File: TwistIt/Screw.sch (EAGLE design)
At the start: 6 parts

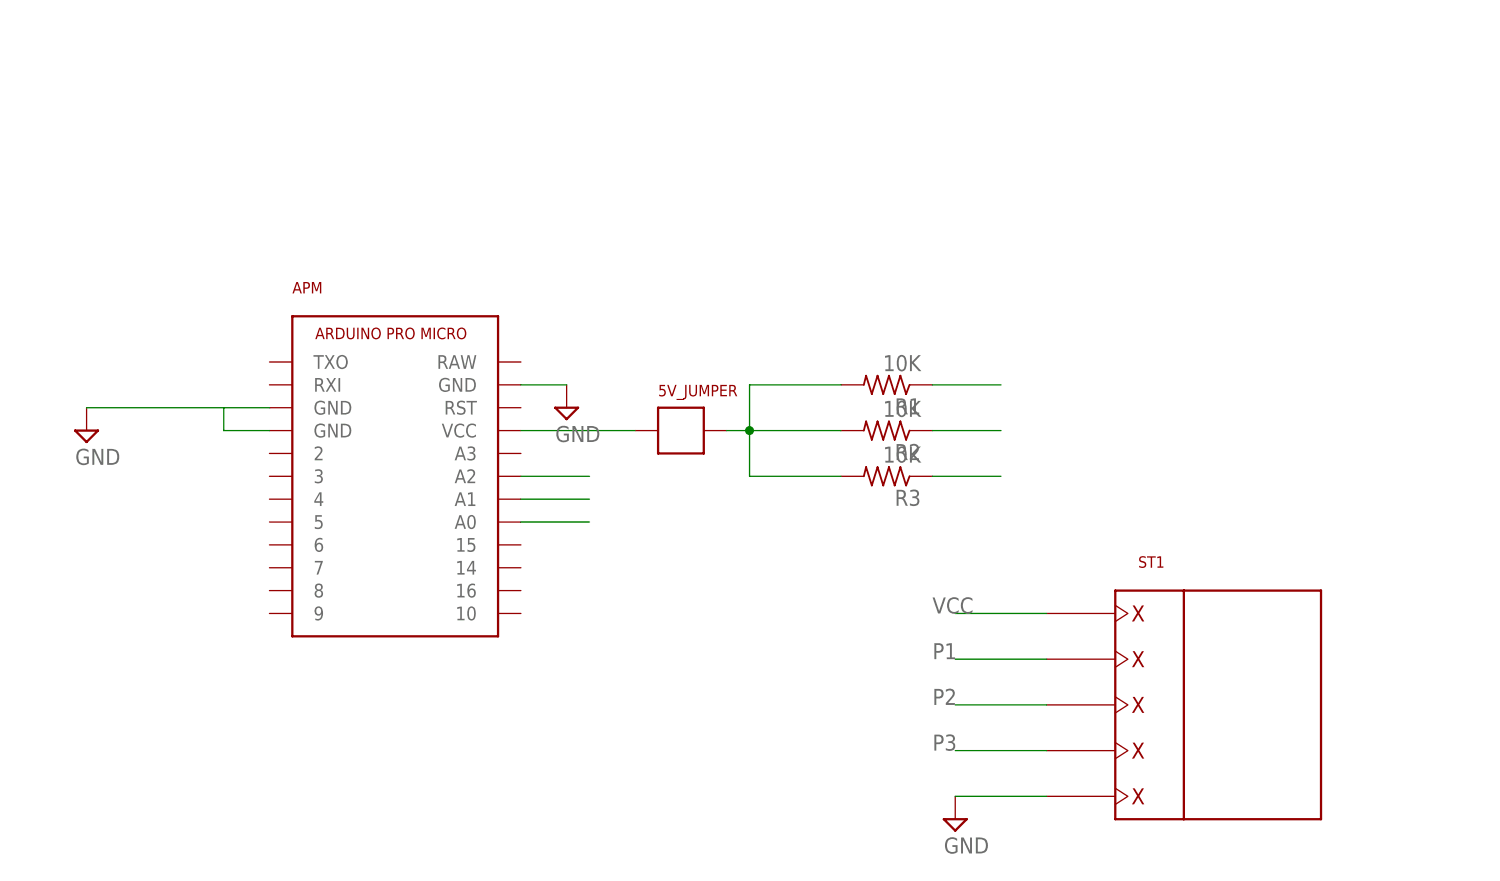
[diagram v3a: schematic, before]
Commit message: Add the yogi bear breakout board
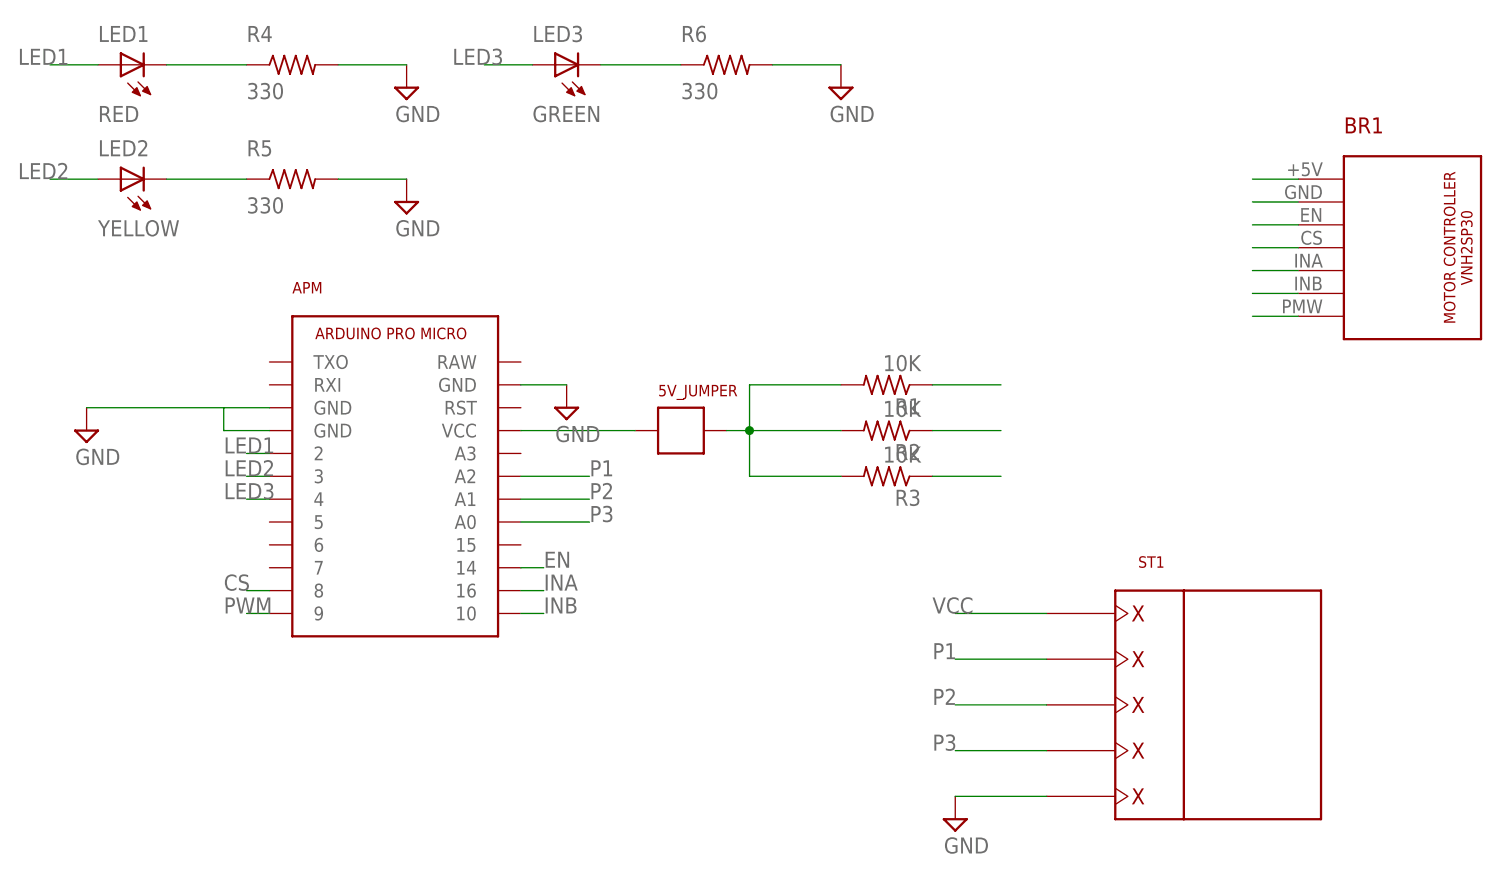
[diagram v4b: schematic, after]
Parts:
- added BR1: VNH2SP30_MOTOR_CONTROLLER, pie:VNH2SP30_MOTOR_CONTROLLER
- added LED1: RED, pie:LED-FKIT-1206
- added LED2: YELLOW, pie:LED-FKIT-1206
- added LED3: GREEN, pie:LED-FKIT-1206
- added R4, R5, R6: 330, pie:R-US_R0603
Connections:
- new net CS: APM.8, BR1.CS
- new net EN: APM.14, BR1.EN
- new net INA: APM.16, BR1.INA
- new net INB: APM.10, BR1.INB
- new net LED1: APM.2, LED1.A
- new net LED2: APM.3, LED2.A
- new net LED3: APM.4, LED3.A
- new net N$2: LED1.C, R4.1
- new net N$4: LED2.C, R5.1
- new net N$6: LED3.C, R6.1
- new net PWM: APM.9, BR1.PMW
- net GND: now also BR1.GND, R4.2, R5.2, R6.2
- net VCC: now also BR1.+5V
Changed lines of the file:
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@@
 <?xml version="1.0" encoding="utf-8"?>
 <!DOCTYPE eagle SYSTEM "eagle.dtd">
-<eagle version="7.6.0">
+<eagle version="7.7.0">
 <drawing>
 <settings>
@@
 <part name="SUPPLY3" library="pie" deviceset="GND" device=""/>
 <part name="5V_JUMPER" library="pie" deviceset="JUMPER" device=""/>
+<part name="BR1" library="pie" deviceset="VNH2SP30_MOTOR_CONTROLLER" device=""/>
+<part name="LED1" library="pie" deviceset="LED" device="-FKIT-1206" value="RED"/>
+<part name="R4" library="pie" deviceset="R-US_" device="R0603" value="330"/>
+<part name="SUPPLY4" library="pie" deviceset="GND" device=""/>
+<part name="LED2" library="pie" deviceset="LED" device="-FKIT-1206" value="YELLOW"/>
+<part name="R5" library="pie" deviceset="R-US_" device="R0603" value="330"/>
+<part name="SUPPLY5" library="pie" deviceset="GND" device=""/>
+<part name="LED3" library="pie" deviceset="LED" device="-FKIT-1206" value="GREEN"/>
+<part name="R6" library="pie" deviceset="R-US_" device="R0603" value="330"/>
+<part name="SUPPLY6" library="pie" deviceset="GND" device=""/>
 </parts>
 <sheets>
@@
 <instance part="SUPPLY3" gate="GND" x="81.28" y="101.6"/>
 <instance part="5V_JUMPER" gate="G$1" x="93.98" y="99.06"/>
+<instance part="BR1" gate="G$1" x="175.26" y="119.38"/>
+<instance part="LED1" gate="G$1" x="33.02" y="139.7"/>
+<instance part="R4" gate="G$1" x="50.8" y="139.7"/>
+<instance part="SUPPLY4" gate="GND" x="63.5" y="137.16"/>
+<instance part="LED2" gate="G$1" x="33.02" y="127"/>
+<instance part="R5" gate="G$1" x="50.8" y="127"/>
+<instance part="SUPPLY5" gate="GND" x="63.5" y="124.46"/>
+<instance part="LED3" gate="G$1" x="81.28" y="139.7"/>
+<instance part="R6" gate="G$1" x="99.06" y="139.7"/>
+<instance part="SUPPLY6" gate="GND" x="111.76" y="137.16"/>
 </instances>
 <busses>
@@
 <wire x1="81.28" y1="104.14" x2="76.2" y2="104.14" width="0.1524" layer="91"/>
 </segment>
+<segment>
+<pinref part="BR1" gate="G$1" pin="GND"/>
+<wire x1="162.56" y1="124.46" x2="157.48" y2="124.46" width="0.1524" layer="91"/>
+</segment>
+<segment>
+<pinref part="R4" gate="G$1" pin="2"/>
+<pinref part="SUPPLY4" gate="GND" pin="GND"/>
+<wire x1="55.88" y1="139.7" x2="63.5" y2="139.7" width="0.1524" layer="91"/>
+</segment>
+<segment>
+<pinref part="R5" gate="G$1" pin="2"/>
+<pinref part="SUPPLY5" gate="GND" pin="GND"/>
+<wire x1="55.88" y1="127" x2="63.5" y2="127" width="0.1524" layer="91"/>
+</segment>
+<segment>
+<pinref part="R6" gate="G$1" pin="2"/>
+<pinref part="SUPPLY6" gate="GND" pin="GND"/>
+<wire x1="104.14" y1="139.7" x2="111.76" y2="139.7" width="0.1524" layer="91"/>
+</segment>
 </net>
 <net name="P1" class="0">
@@
 <pinref part="APM" gate="G$1" pin="A2"/>
 <wire x1="76.2" y1="93.98" x2="83.82" y2="93.98" width="0.1524" layer="91"/>
+<label x="83.82" y="93.98" size="1.778" layer="95"/>
 </segment>
 </net>
@@
 <pinref part="5V_JUMPER" gate="G$1" pin="P$1"/>
 </segment>
+<segment>
+<pinref part="BR1" gate="G$1" pin="+5V"/>
+<wire x1="162.56" y1="127" x2="157.48" y2="127" width="0.1524" layer="91"/>
+</segment>
 </net>
 <net name="P2" class="0">
@@
 <pinref part="APM" gate="G$1" pin="A1"/>
 <wire x1="76.2" y1="91.44" x2="83.82" y2="91.44" width="0.1524" layer="91"/>
+<label x="83.82" y="91.44" size="1.778" layer="95"/>
 </segment>
 <segment>
@@
 <pinref part="APM" gate="G$1" pin="A0"/>
 <wire x1="76.2" y1="88.9" x2="83.82" y2="88.9" width="0.1524" layer="91"/>
+<label x="83.82" y="88.9" size="1.778" layer="95"/>
 </segment>
 <segment>
 <pinref part="R3" gate="G$1" pin="1"/>
 <wire x1="121.92" y1="93.98" x2="129.54" y2="93.98" width="0.1524" layer="91"/>
+</segment>
+</net>
+<net name="EN" class="0">
+<segment>
+<pinref part="BR1" gate="G$1" pin="EN"/>
+<wire x1="162.56" y1="121.92" x2="157.48" y2="121.92" width="0.1524" layer="91"/>
+</segment>
+<segment>
+<pinref part="APM" gate="G$1" pin="14"/>
+<wire x1="76.2" y1="83.82" x2="78.74" y2="83.82" width="0.1524" layer="91"/>
+<label x="78.74" y="83.82" size="1.778" layer="95"/>
+</segment>
+</net>
+<net name="CS" class="0">
+<segment>
+<pinref part="BR1" gate="G$1" pin="CS"/>
+<wire x1="162.56" y1="119.38" x2="157.48" y2="119.38" width="0.1524" layer="91"/>
+</segment>
+<segment>
+<pinref part="APM" gate="G$1" pin="8"/>
+<wire x1="48.26" y1="81.28" x2="45.72" y2="81.28" width="0.1524" layer="91"/>
+<label x="43.18" y="81.28" size="1.778" layer="95"/>
+</segment>
+</net>
+<net name="INA" class="0">
+<segment>
+<pinref part="BR1" gate="G$1" pin="INA"/>
+<wire x1="162.56" y1="116.84" x2="157.48" y2="116.84" width="0.1524" layer="91"/>
+</segment>
+<segment>
+<pinref part="APM" gate="G$1" pin="16"/>
+<wire x1="76.2" y1="81.28" x2="78.74" y2="81.28" width="0.1524" layer="91"/>
+<label x="78.74" y="81.28" size="1.778" layer="95"/>
+</segment>
+</net>
+<net name="INB" class="0">
+<segment>
+<pinref part="BR1" gate="G$1" pin="INB"/>
+<wire x1="162.56" y1="114.3" x2="157.48" y2="114.3" width="0.1524" layer="91"/>
+</segment>
+<segment>
+<pinref part="APM" gate="G$1" pin="10"/>
+<wire x1="76.2" y1="78.74" x2="78.74" y2="78.74" width="0.1524" layer="91"/>
+<label x="78.74" y="78.74" size="1.778" layer="95"/>
+</segment>
+</net>
+<net name="PWM" class="0">
+<segment>
+<pinref part="BR1" gate="G$1" pin="PMW"/>
+<wire x1="162.56" y1="111.76" x2="157.48" y2="111.76" width="0.1524" layer="91"/>
+</segment>
+<segment>
+<pinref part="APM" gate="G$1" pin="9"/>
+<wire x1="48.26" y1="78.74" x2="45.72" y2="78.74" width="0.1524" layer="91"/>
+<label x="43.18" y="78.74" size="1.778" layer="95"/>
+</segment>
+</net>
+<net name="LED1" class="0">
+<segment>
+<pinref part="LED1" gate="G$1" pin="A"/>
+<wire x1="29.21" y1="139.7" x2="23.876" y2="139.7" width="0.1524" layer="91"/>
+<label x="20.32" y="139.7" size="1.778" layer="95"/>
+</segment>
+<segment>
+<pinref part="APM" gate="G$1" pin="2"/>
+<wire x1="48.26" y1="96.52" x2="45.72" y2="96.52" width="0.1524" layer="91"/>
+<label x="43.18" y="96.52" size="1.778" layer="95"/>
+</segment>
+</net>
+<net name="LED2" class="0">
+<segment>
+<pinref part="LED2" gate="G$1" pin="A"/>
+<wire x1="29.21" y1="127" x2="23.876" y2="127" width="0.1524" layer="91"/>
+<label x="20.32" y="127" size="1.778" layer="95"/>
+</segment>
+<segment>
+<pinref part="APM" gate="G$1" pin="3"/>
+<wire x1="48.26" y1="93.98" x2="45.72" y2="93.98" width="0.1524" layer="91"/>
+<label x="43.18" y="93.98" size="1.778" layer="95"/>
+</segment>
+</net>
+<net name="LED3" class="0">
+<segment>
+<pinref part="LED3" gate="G$1" pin="A"/>
+<wire x1="77.47" y1="139.7" x2="72.136" y2="139.7" width="0.1524" layer="91"/>
+<label x="68.58" y="139.7" size="1.778" layer="95"/>
+</segment>
+<segment>
+<pinref part="APM" gate="G$1" pin="4"/>
+<wire x1="48.26" y1="91.44" x2="45.72" y2="91.44" width="0.1524" layer="91"/>
+<label x="43.18" y="91.44" size="1.778" layer="95"/>
+</segment>
+</net>
+<net name="N$2" class="0">
+<segment>
+<pinref part="LED1" gate="G$1" pin="C"/>
+<pinref part="R4" gate="G$1" pin="1"/>
+<wire x1="36.83" y1="139.7" x2="45.72" y2="139.7" width="0.1524" layer="91"/>
+</segment>
+</net>
+<net name="N$4" class="0">
+<segment>
+<pinref part="LED2" gate="G$1" pin="C"/>
+<pinref part="R5" gate="G$1" pin="1"/>
+<wire x1="36.83" y1="127" x2="45.72" y2="127" width="0.1524" layer="91"/>
+</segment>
+</net>
+<net name="N$6" class="0">
+<segment>
+<pinref part="LED3" gate="G$1" pin="C"/>
+<pinref part="R6" gate="G$1" pin="1"/>
+<wire x1="85.09" y1="139.7" x2="93.98" y2="139.7" width="0.1524" layer="91"/>
 </segment>
 </net>
@@
 </schematic>
 </drawing>
+<compatibility>
+<note version="6.3" minversion="6.2.2" severity="warning">
+Since Version 6.2.2 text objects can contain more than one line,
+which will not be processed correctly with this version.
+</note>
+</compatibility>
 </eagle>
